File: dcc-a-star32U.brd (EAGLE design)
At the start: 25.4 x 15.2 mm, 8 parts, among them Q1 MOSFET-NCHANNEL2N7002PW

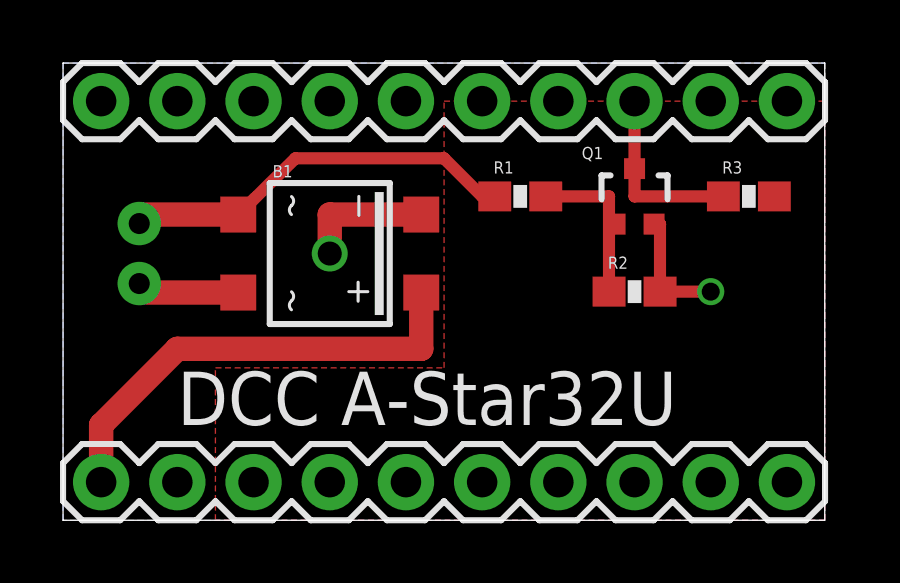
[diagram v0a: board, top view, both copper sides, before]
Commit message: fabbed version
increase padding, minor tweaks
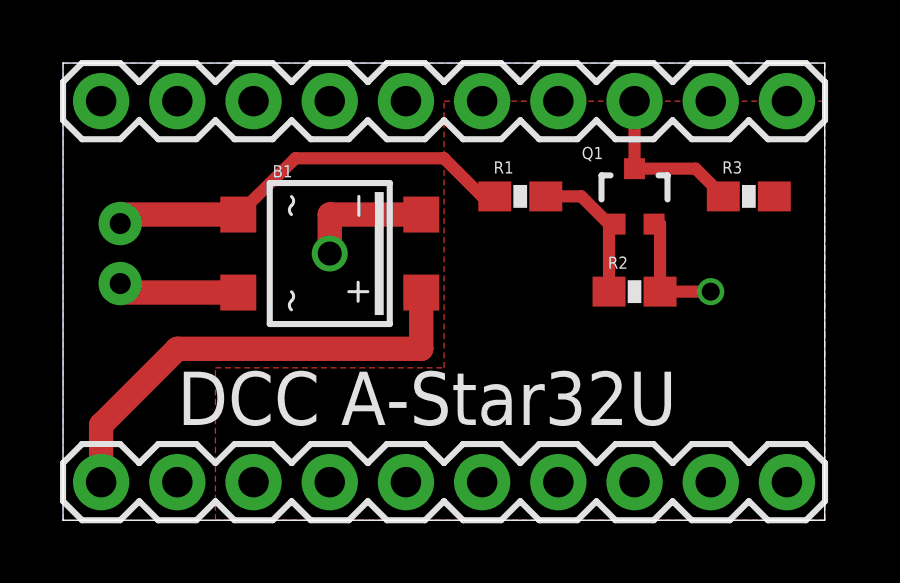
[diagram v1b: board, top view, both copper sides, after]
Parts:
- moved DCC-IN 0.64 mm to (1.91, 11.4)
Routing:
- net N$3: track 13.4 -> 14.1 mm
- net N$4: track 3.63 -> 4.23 mm
- net N$1: track 5.48 -> 4.94 mm
- net DCC-INT: track 6.14 -> 5.59 mm
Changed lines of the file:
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@@
 </autorouter>
 <elements>
-<element name="DCC-IN" library="SparkFun-Connectors" package="JST-2-PTH-NS" value="M02-JST-2-PTH-NO_SILK" x="2.54" y="11.43" smashed="yes" rot="R90"/>
+<element name="DCC-IN" library="SparkFun-Connectors" package="JST-2-PTH-NS" value="M02-JST-2-PTH-NO_SILK" x="1.905" y="11.43" smashed="yes" rot="R90"/>
 <element name="B1" library="rectifier" package="SOIC-4" value="MB1S" x="8.89" y="11.43" smashed="yes" rot="R270">
 <attribute name="NAME" x="6.985" y="13.97" size="0.4064" layer="25" font="vector"/>
@@
 <signals>
 <signal name="GND">
-<polygon width="0.4064" layer="16" isolate="0.381">
+<polygon width="0.4064" layer="16" isolate="0.508">
 <vertex x="0" y="17.78"/>
 <vertex x="25.4" y="17.78"/>
@@
 <contactref element="Q1" pad="3"/>
 <contactref element="R3" pad="1"/>
-<wire x1="19.05" y1="14.26" x2="19.05" y2="13.335" width="0.4064" layer="1"/>
-<wire x1="19.05" y1="13.335" x2="22.01" y2="13.335" width="0.4064" layer="1"/>
 <contactref element="JP1" pad="8"/>
 <wire x1="19.05" y1="14.26" x2="19.05" y2="16.51" width="0.4064" layer="1"/>
+<wire x1="19.05" y1="14.26" x2="21.085" y2="14.26" width="0.4064" layer="1"/>
+<wire x1="21.085" y1="14.26" x2="22.01" y2="13.335" width="0.4064" layer="1"/>
 </signal>
 <signal name="5V">
-<polygon width="0.4064" layer="1" isolate="0.381">
+<polygon width="0.4064" layer="1" isolate="0.508">
 <vertex x="12.7" y="16.51"/>
 <vertex x="25.4" y="16.51"/>
@@
 <wire x1="12.7" y1="14.605" x2="7.745" y2="14.605" width="0.4064" layer="1"/>
 <wire x1="7.745" y1="14.605" x2="5.84" y2="12.73" width="0.4064" layer="1"/>
-<wire x1="5.84" y1="12.73" x2="2.57" y2="12.73" width="0.8128" layer="1"/>
-<wire x1="2.57" y1="12.73" x2="2.54" y2="12.43" width="0.8128" layer="1"/>
+<wire x1="5.84" y1="12.73" x2="1.935" y2="12.73" width="0.8128" layer="1"/>
+<wire x1="1.935" y1="12.73" x2="1.905" y2="12.43" width="0.8128" layer="1"/>
 </signal>
 <signal name="N$4">
 <contactref element="B1" pad="~2"/>
 <contactref element="DCC-IN" pad="1"/>
-<wire x1="5.84" y1="10.13" x2="2.51" y2="10.13" width="0.8128" layer="1"/>
-<wire x1="2.51" y1="10.13" x2="2.54" y2="10.43" width="0.8128" layer="1"/>
+<wire x1="5.84" y1="10.13" x2="1.905" y2="10.13" width="0.8128" layer="1"/>
+<wire x1="1.905" y1="10.13" x2="1.905" y2="10.43" width="0.8128" layer="1"/>
 </signal>
 <signal name="N$1">
@@
 <contactref element="Q1" pad="1"/>
 <contactref element="R2" pad="1"/>
-<wire x1="16.09" y1="13.335" x2="18.2" y2="13.335" width="0.4064" layer="1"/>
-<wire x1="18.2" y1="13.335" x2="18.2" y2="12.41" width="0.4064" layer="1"/>
+<wire x1="16.09" y1="13.335" x2="17.275" y2="13.335" width="0.4064" layer="1"/>
 <wire x1="18.2" y1="12.41" x2="18.2" y2="10.16" width="0.4064" layer="1"/>
 <wire x1="18.4" y1="12.41" x2="18.2" y2="12.41" width="0.4064" layer="1"/>
+<wire x1="18.2" y1="12.41" x2="17.275" y2="13.335" width="0.4064" layer="1"/>
 </signal>
 </signals>
